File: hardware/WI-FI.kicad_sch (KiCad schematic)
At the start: 18 parts, among them Y2 26МHz

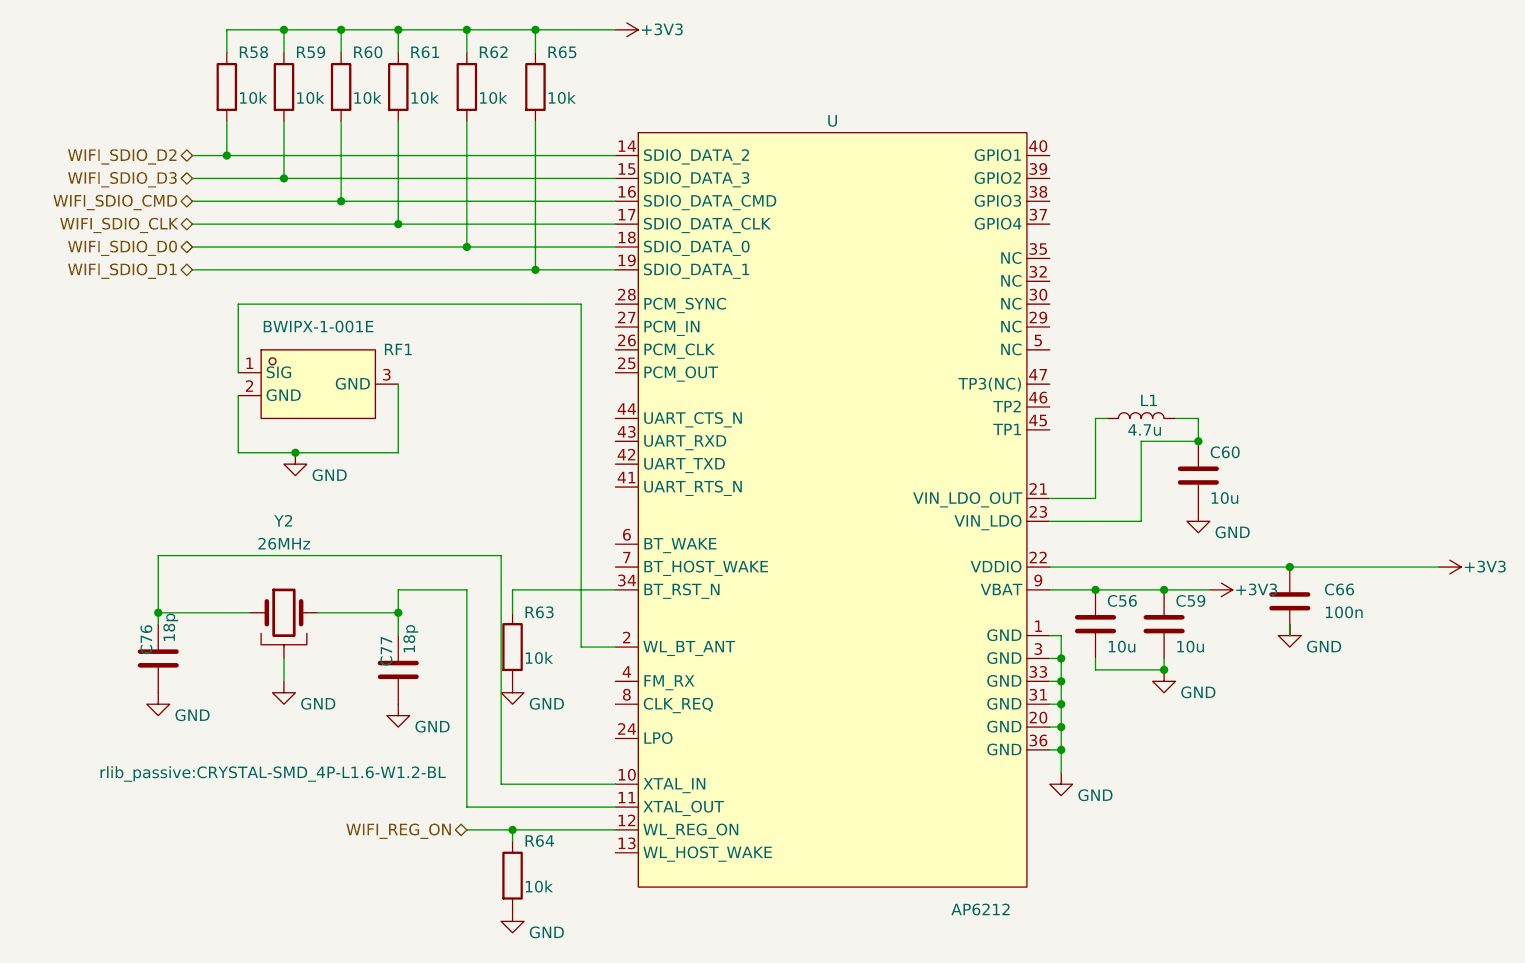
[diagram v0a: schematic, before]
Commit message: some changes on fab layers
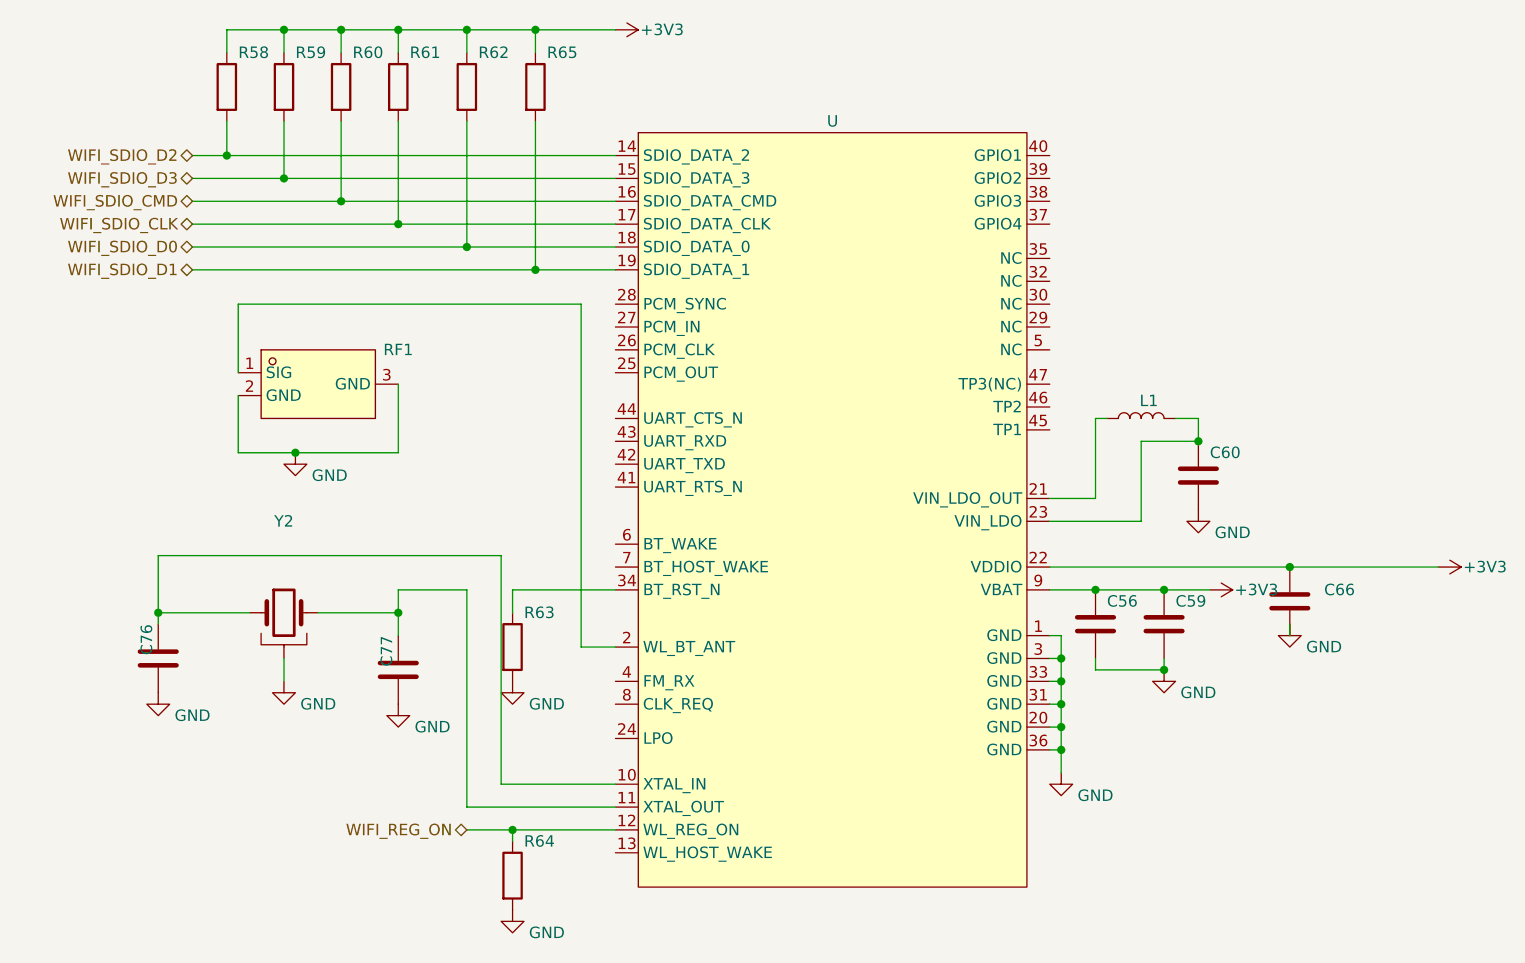
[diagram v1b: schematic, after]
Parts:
- C56, C59, C60: value 10u -> (none); footprint rlib_passive:C_0603_1608Metric -> (none)
- C66: value 100n -> (none); footprint rlib_passive:C_0603_1608Metric -> (none)
- C76, C77: value 18p -> (none); footprint rlib_passive:C_0603_1608Metric -> (none)
- L1: value 4.7u -> (none); footprint rlib_passive:IND_LQH32PN4R7NN0L -> (none)
- R58, R59, R60, R61, R62, R63, R64, R65: value 10k -> (none); footprint rlib_passive:R_0603_1608Metric -> (none)
- RF1: value BWIPX-1-001E -> (none); footprint rlib_connectors:IPEX-SMD_BWIPX-1-001E -> (none)
- Y2: value 26МHz -> (none); footprint rlib_passive:CRYSTAL-SMD_4P-L1.6-W1.2-BL -> (none)
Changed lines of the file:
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@@
       (effects (font (size 1.27 1.27)) (justify left))
     )
-    (property "Value" "10k" (id 1) (at 111.76 105.41 0)
-      (effects (font (size 1.27 1.27)) (justify left))
-    )
-    (property "Footprint" "rlib_passive:R_0603_1608Metric" (id 2) (at 108.712 104.14 90)
+    (property "Value" "" (id 1) (at 111.76 105.41 0)
+      (effects (font (size 1.27 1.27)) (justify left))
+    )
+    (property "Footprint" "" (id 2) (at 108.712 104.14 90)
       (effects (font (size 1.27 1.27)) hide)
     )
@@
       (effects (font (size 1.27 1.27)) (justify left))
     )
-    (property "Value" "10k" (id 1) (at 111.76 130.81 0)
-      (effects (font (size 1.27 1.27)) (justify left))
-    )
-    (property "Footprint" "rlib_passive:R_0603_1608Metric" (id 2) (at 108.712 129.54 90)
+    (property "Value" "" (id 1) (at 111.76 130.81 0)
+      (effects (font (size 1.27 1.27)) (justify left))
+    )
+    (property "Footprint" "" (id 2) (at 108.712 129.54 90)
       (effects (font (size 1.27 1.27)) hide)
     )
@@
     (in_bom yes) (on_board yes)
     (property "Reference" "U12" (id 0) (at 146.05 45.72 0))
-    (property "Value" "AP6212" (id 1) (at 162.56 133.35 0))
-    (property "Footprint" "rlib_modules:QFN-44_L12.0-W12.0-P0.90-TL_AP6212" (id 2) (at 146.05 115.57 0)
+    (property "Value" "" (id 1) (at 162.56 133.35 0))
+    (property "Footprint" "" (id 2) (at 146.05 115.57 0)
       (effects (font (size 1.27 1.27)) hide)
     )
@@
     (in_bom yes) (on_board yes)
     (property "Reference" "RF1" (id 0) (at 97.79 71.12 0))
-    (property "Value" "BWIPX-1-001E" (id 1) (at 88.9 68.58 0))
-    (property "Footprint" "rlib_connectors:IPEX-SMD_BWIPX-1-001E" (id 2) (at 88.9 83.82 0)
+    (property "Value" "" (id 1) (at 88.9 68.58 0))
+    (property "Footprint" "" (id 2) (at 88.9 83.82 0)
       (effects (font (size 1.27 1.27)) hide)
     )
@@
     (in_bom yes) (on_board yes)
     (property "Reference" "Y2" (id 0) (at 85.09 90.17 0))
-    (property "Value" "26МHz" (id 1) (at 85.09 92.71 0))
-    (property "Footprint" "rlib_passive:CRYSTAL-SMD_4P-L1.6-W1.2-BL" (id 2) (at 83.82 118.11 0))
+    (property "Value" "" (id 1) (at 85.09 92.71 0))
+    (property "Footprint" "" (id 2) (at 83.82 118.11 0))
     (property "Datasheet" "~" (id 3) (at 95.25 113.03 0)
       (effects (font (size 1.27 1.27)) hide)
@@
       (effects (font (size 1.27 1.27)) (justify left))
     )
-    (property "Value" "100n" (id 1) (at 200.66 100.3299 0)
-      (effects (font (size 1.27 1.27)) (justify left))
-    )
-    (property "Footprint" "rlib_passive:C_0603_1608Metric" (id 2) (at 197.8152 102.87 0)
+    (property "Value" "" (id 1) (at 200.66 100.3299 0)
+      (effects (font (size 1.27 1.27)) (justify left))
+    )
+    (property "Footprint" "" (id 2) (at 197.8152 102.87 0)
       (effects (font (size 1.27 1.27)) hide)
     )
@@
       (effects (font (size 1.27 1.27)) (justify left))
     )
-    (property "Value" "10u" (id 1) (at 184.15 104.14 0)
-      (effects (font (size 1.27 1.27)) (justify left))
-    )
-    (property "Footprint" "rlib_passive:C_0603_1608Metric" (id 2) (at 183.8452 105.41 0)
+    (property "Value" "" (id 1) (at 184.15 104.14 0)
+      (effects (font (size 1.27 1.27)) (justify left))
+    )
+    (property "Footprint" "" (id 2) (at 183.8452 105.41 0)
       (effects (font (size 1.27 1.27)) hide)
     )
@@
     (in_bom yes) (on_board yes)
     (property "Reference" "L1" (id 0) (at 181.1924 76.7822 90))
-    (property "Value" "4.7u" (id 1) (at 180.7551 80.0615 90))
-    (property "Footprint" "rlib_passive:IND_LQH32PN4R7NN0L" (id 2) (at 180.34 78.74 0)
+    (property "Value" "" (id 1) (at 180.7551 80.0615 90))
+    (property "Footprint" "" (id 2) (at 180.34 78.74 0)
       (effects (font (size 1.27 1.27)) hide)
     )
@@
       (effects (font (size 1.27 1.27)) (justify left))
     )
-    (property "Value" "10k" (id 1) (at 86.36 43.18 0)
-      (effects (font (size 1.27 1.27)) (justify left))
-    )
-    (property "Footprint" "rlib_passive:R_0603_1608Metric" (id 2) (at 83.312 41.91 90)
+    (property "Value" "" (id 1) (at 86.36 43.18 0)
+      (effects (font (size 1.27 1.27)) (justify left))
+    )
+    (property "Footprint" "" (id 2) (at 83.312 41.91 90)
       (effects (font (size 1.27 1.27)) hide)
     )
@@
       (effects (font (size 1.27 1.27)) (justify left))
     )
-    (property "Value" "10k" (id 1) (at 106.68 43.18 0)
-      (effects (font (size 1.27 1.27)) (justify left))
-    )
-    (property "Footprint" "rlib_passive:R_0603_1608Metric" (id 2) (at 103.632 41.91 90)
+    (property "Value" "" (id 1) (at 106.68 43.18 0)
+      (effects (font (size 1.27 1.27)) (justify left))
+    )
+    (property "Footprint" "" (id 2) (at 103.632 41.91 90)
       (effects (font (size 1.27 1.27)) hide)
     )
@@
       (effects (font (size 1.27 1.27)) (justify left))
     )
-    (property "Value" "10u" (id 1) (at 176.53 104.14 0)
-      (effects (font (size 1.27 1.27)) (justify left))
-    )
-    (property "Footprint" "rlib_passive:C_0603_1608Metric" (id 2) (at 176.2252 105.41 0)
+    (property "Value" "" (id 1) (at 176.53 104.14 0)
+      (effects (font (size 1.27 1.27)) (justify left))
+    )
+    (property "Footprint" "" (id 2) (at 176.2252 105.41 0)
       (effects (font (size 1.27 1.27)) hide)
     )
@@
       (effects (font (size 1.27 1.27)) (justify left))
     )
-    (property "Value" "10k" (id 1) (at 99.06 43.18 0)
-      (effects (font (size 1.27 1.27)) (justify left))
-    )
-    (property "Footprint" "rlib_passive:R_0603_1608Metric" (id 2) (at 96.012 41.91 90)
+    (property "Value" "" (id 1) (at 99.06 43.18 0)
+      (effects (font (size 1.27 1.27)) (justify left))
+    )
+    (property "Footprint" "" (id 2) (at 96.012 41.91 90)
       (effects (font (size 1.27 1.27)) hide)
     )
@@
       (effects (font (size 1.27 1.27)) (justify left))
     )
-    (property "Value" "10u" (id 1) (at 187.96 87.63 0)
-      (effects (font (size 1.27 1.27)) (justify left))
-    )
-    (property "Footprint" "rlib_passive:C_0603_1608Metric" (id 2) (at 187.6552 88.9 0)
+    (property "Value" "" (id 1) (at 187.96 87.63 0)
+      (effects (font (size 1.27 1.27)) (justify left))
+    )
+    (property "Footprint" "" (id 2) (at 187.6552 88.9 0)
       (effects (font (size 1.27 1.27)) hide)
     )
@@
       (effects (font (size 1.27 1.27)) (justify left))
     )
-    (property "Value" "18p" (id 1) (at 99.06 101.6 90)
-      (effects (font (size 1.27 1.27)) (justify left))
-    )
-    (property "Footprint" "rlib_passive:C_0603_1608Metric" (id 2) (at 96.8248 102.87 0)
+    (property "Value" "" (id 1) (at 99.06 101.6 90)
+      (effects (font (size 1.27 1.27)) (justify left))
+    )
+    (property "Footprint" "" (id 2) (at 96.8248 102.87 0)
       (effects (font (size 1.27 1.27)) hide)
     )
@@
       (effects (font (size 1.27 1.27)) (justify left))
     )
-    (property "Value" "10k" (id 1) (at 80.01 43.18 0)
-      (effects (font (size 1.27 1.27)) (justify left))
-    )
-    (property "Footprint" "rlib_passive:R_0603_1608Metric" (id 2) (at 76.962 41.91 90)
+    (property "Value" "" (id 1) (at 80.01 43.18 0)
+      (effects (font (size 1.27 1.27)) (justify left))
+    )
+    (property "Footprint" "" (id 2) (at 76.962 41.91 90)
       (effects (font (size 1.27 1.27)) hide)
     )
@@
       (effects (font (size 1.27 1.27)) (justify left))
     )
-    (property "Value" "10k" (id 1) (at 92.71 43.18 0)
-      (effects (font (size 1.27 1.27)) (justify left))
-    )
-    (property "Footprint" "rlib_passive:R_0603_1608Metric" (id 2) (at 89.662 41.91 90)
+    (property "Value" "" (id 1) (at 92.71 43.18 0)
+      (effects (font (size 1.27 1.27)) (justify left))
+    )
+    (property "Footprint" "" (id 2) (at 89.662 41.91 90)
       (effects (font (size 1.27 1.27)) hide)
     )
@@
       (effects (font (size 1.27 1.27)) (justify left))
     )
-    (property "Value" "18p" (id 1) (at 72.39 100.33 90)
-      (effects (font (size 1.27 1.27)) (justify left))
-    )
-    (property "Footprint" "rlib_passive:C_0603_1608Metric" (id 2) (at 70.1548 101.6 0)
+    (property "Value" "" (id 1) (at 72.39 100.33 90)
+      (effects (font (size 1.27 1.27)) (justify left))
+    )
+    (property "Footprint" "" (id 2) (at 70.1548 101.6 0)
       (effects (font (size 1.27 1.27)) hide)
     )
@@
       (effects (font (size 1.27 1.27)) (justify left))
     )
-    (property "Value" "10k" (id 1) (at 114.3 43.18 0)
-      (effects (font (size 1.27 1.27)) (justify left))
-    )
-    (property "Footprint" "rlib_passive:R_0603_1608Metric" (id 2) (at 111.252 41.91 90)
-      (effects (font (size 1.27 1.27)) hide)
-    )
+    (property "Value" "" (id 1) (at 114.3 43.18 0)
+      (effects (font (size 1.27 1.27)) (justify left))
+    )
+    (property "Footprint" "" (id 2) (at 111.252 41.91 90)
+      (effects (font (size 1.27 1.27)) hide)
+    )

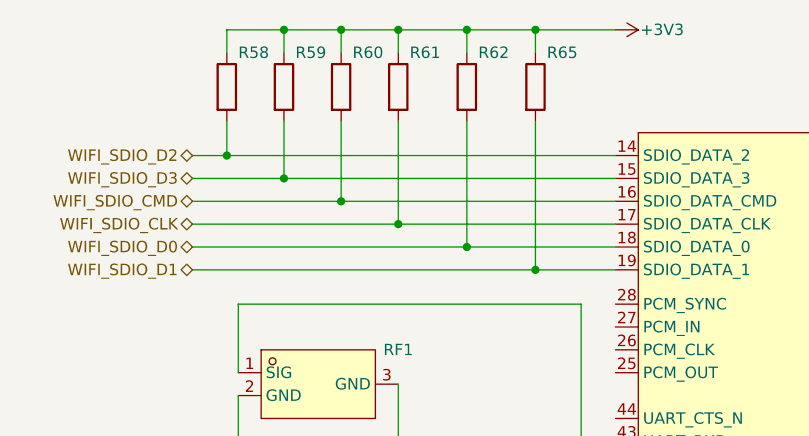
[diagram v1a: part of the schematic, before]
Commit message: pwr btn is optional connected to soc
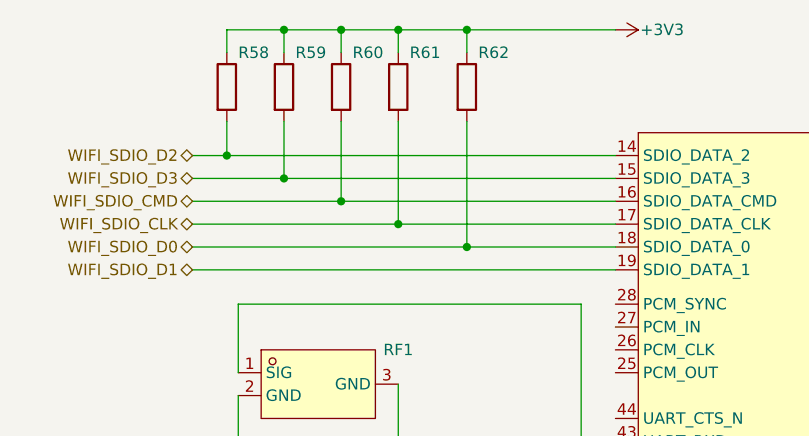
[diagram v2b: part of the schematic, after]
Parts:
- removed R65: (no value), symbol rlib_passive:R
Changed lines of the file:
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@@
   (junction (at 78.74 49.53) (diameter 0) (color 0 0 0 0)
   )
-  (junction (at 113.03 35.56) (diameter 0) (color 0 0 0 0)
-  )
   (junction (at 171.45 115.57) (diameter 0) (color 0 0 0 0)
   )
@@
   (junction (at 86.36 82.55) (diameter 0) (color 0 0 0 0)
   )
-  (junction (at 113.03 62.23) (diameter 0) (color 0 0 0 0)
-  )
   (junction (at 97.79 100.33) (diameter 0) (color 0 0 0 0)
   )
@@
     (stroke (width 0) (type default) (color 0 0 0 0))
   )
-  (wire (pts (xy 113.03 35.56) (xy 121.92 35.56))
-    (stroke (width 0) (type default) (color 0 0 0 0))
-  )
   (wire (pts (xy 105.41 59.69) (xy 121.92 59.69))
     (stroke (width 0) (type default) (color 0 0 0 0))
@@
     (stroke (width 0) (type default) (color 0 0 0 0))
   )
-  (wire (pts (xy 113.03 62.23) (xy 121.92 62.23))
-    (stroke (width 0) (type default) (color 0 0 0 0))
-  )
-  (wire (pts (xy 113.03 45.72) (xy 113.03 62.23))
+  (wire (pts (xy 74.93 62.23) (xy 121.92 62.23))
     (stroke (width 0) (type default) (color 0 0 0 0))
   )
@@
     (stroke (width 0) (type default) (color 0 0 0 0))
   )
-  (wire (pts (xy 74.93 62.23) (xy 113.03 62.23))
-    (stroke (width 0) (type default) (color 0 0 0 0))
-  )
-  (wire (pts (xy 105.41 35.56) (xy 113.03 35.56))
+  (wire (pts (xy 105.41 35.56) (xy 121.92 35.56))
     (stroke (width 0) (type default) (color 0 0 0 0))
   )
@@
   )
   (wire (pts (xy 118.11 104.14) (xy 121.92 104.14))
-    (stroke (width 0) (type default) (color 0 0 0 0))
-  )
-  (wire (pts (xy 113.03 35.56) (xy 113.03 38.1))
     (stroke (width 0) (type default) (color 0 0 0 0))
   )
@@
     (pin "1")
   )
-  (symbol (lib_id "rlib_passive:R") (at 113.03 41.91 0) (unit 1)
-    (in_bom yes) (on_board yes)
-    (property "Reference" "R65" (id 0) (at 114.3 38.1 0)
-      (effects (font (size 1.27 1.27)) (justify left))
-    )
-    (property "Value" "" (id 1) (at 114.3 43.18 0)
-      (effects (font (size 1.27 1.27)) (justify left))
-    )
-    (property "Footprint" "" (id 2) (at 111.252 41.91 90)
-      (effects (font (size 1.27 1.27)) hide)
-    )
-    (property "Datasheet" "~" (id 3) (at 113.03 41.91 0)
-      (effects (font (size 1.27 1.27)) hide)
-    )
-    (property "Tolerance" "1%" (id 4) (at 113.03 41.91 0)
-      (effects (font (size 1.27 1.27)) hide)
-    )
-    (property "Manufacturer" "Viking Tech" (id 6) (at 113.03 41.91 0)
-      (effects (font (size 1.27 1.27)) hide)
-    )
-    (property "Mnfct.  partnumber" "" (id 7) (at 113.03 41.91 0)
-      (effects (font (size 1.27 1.27)) hide)
-    )
-    (property "LCSC Partnumber" "" (id 8) (at 113.03 41.91 0)
-      (effects (font (size 1.27 1.27)) hide)
-    )
-    (property "LCSC partnumber" "C217687" (id 9) (at 113.03 41.91 0)
-      (effects (font (size 1.27 1.27)) hide)
-    )
-    (property "Mnfct. partnumber" "ARG03FTC1002" (id 10) (at 113.03 41.91 0)
-      (effects (font (size 1.27 1.27)) hide)
-    )
-    (pin "1")
-    (pin "2")
-  )
 )
